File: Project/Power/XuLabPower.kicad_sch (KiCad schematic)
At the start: 24 parts, among them J1 Servo, J2 Servo, J3 Servo, J4 Servo, J5 Servo, J6 Servo, J7 Servo, J8 Servo, Q1 SQJ138ELP, Q2 SQJ138ELP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

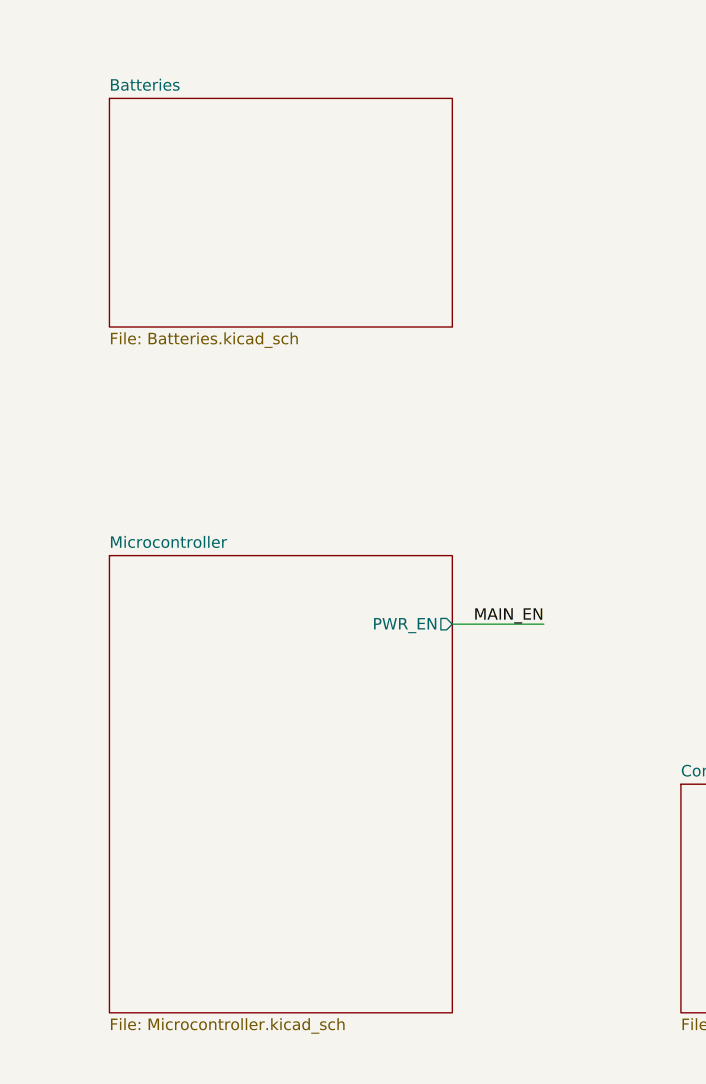
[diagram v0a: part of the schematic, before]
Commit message: Add INA226 sensors for batteries
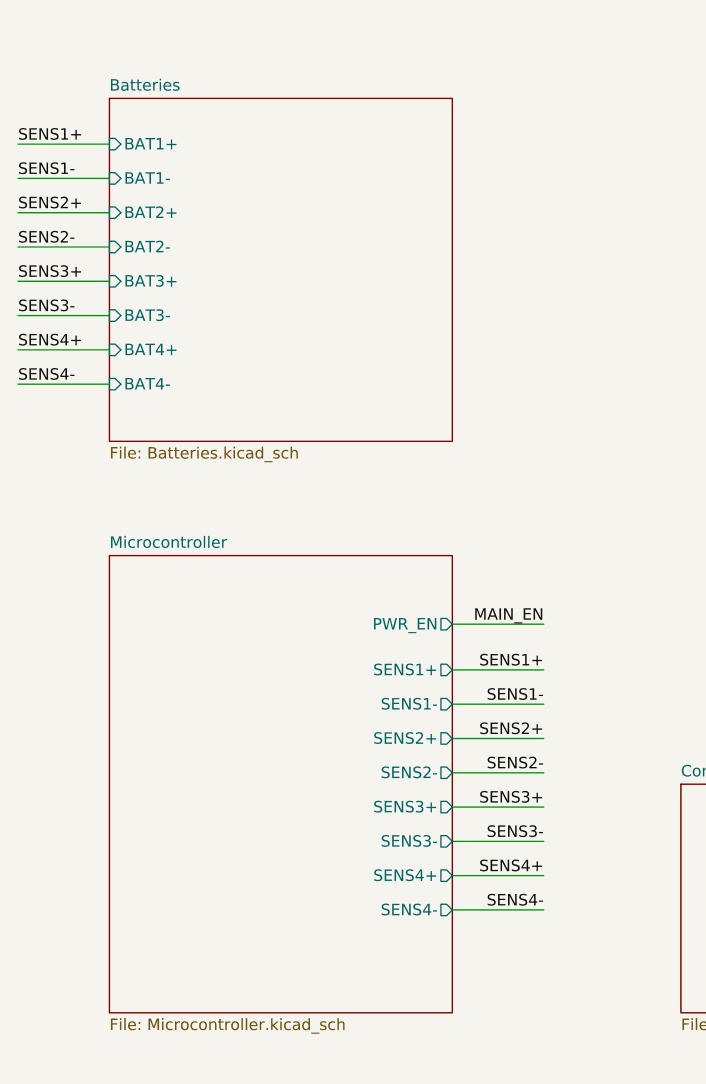
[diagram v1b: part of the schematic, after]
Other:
- sheet Batteries ports: added BAT1+, BAT1-, BAT2+, BAT2-, BAT3+, BAT3-, BAT4+, BAT4-; removed none
- sheet Microcontroller ports: added SENS1+, SENS1-, SENS2+, SENS2-, SENS3+, SENS3-, SENS4+, SENS4-; removed none

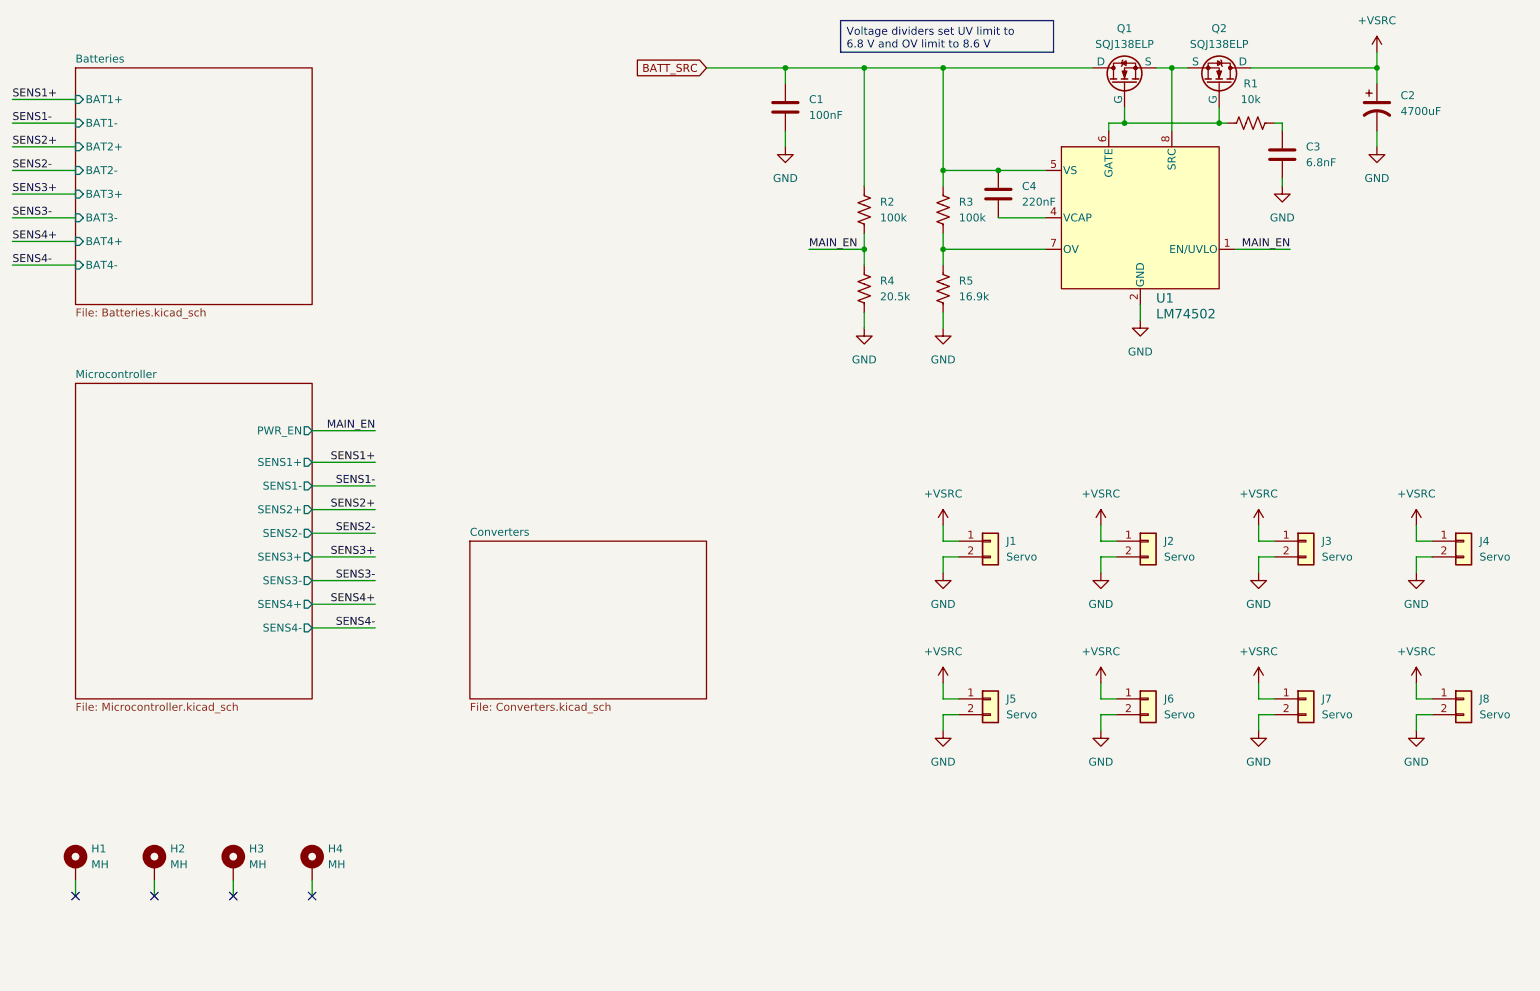
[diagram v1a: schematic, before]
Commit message: Add more sensors for fin module servos
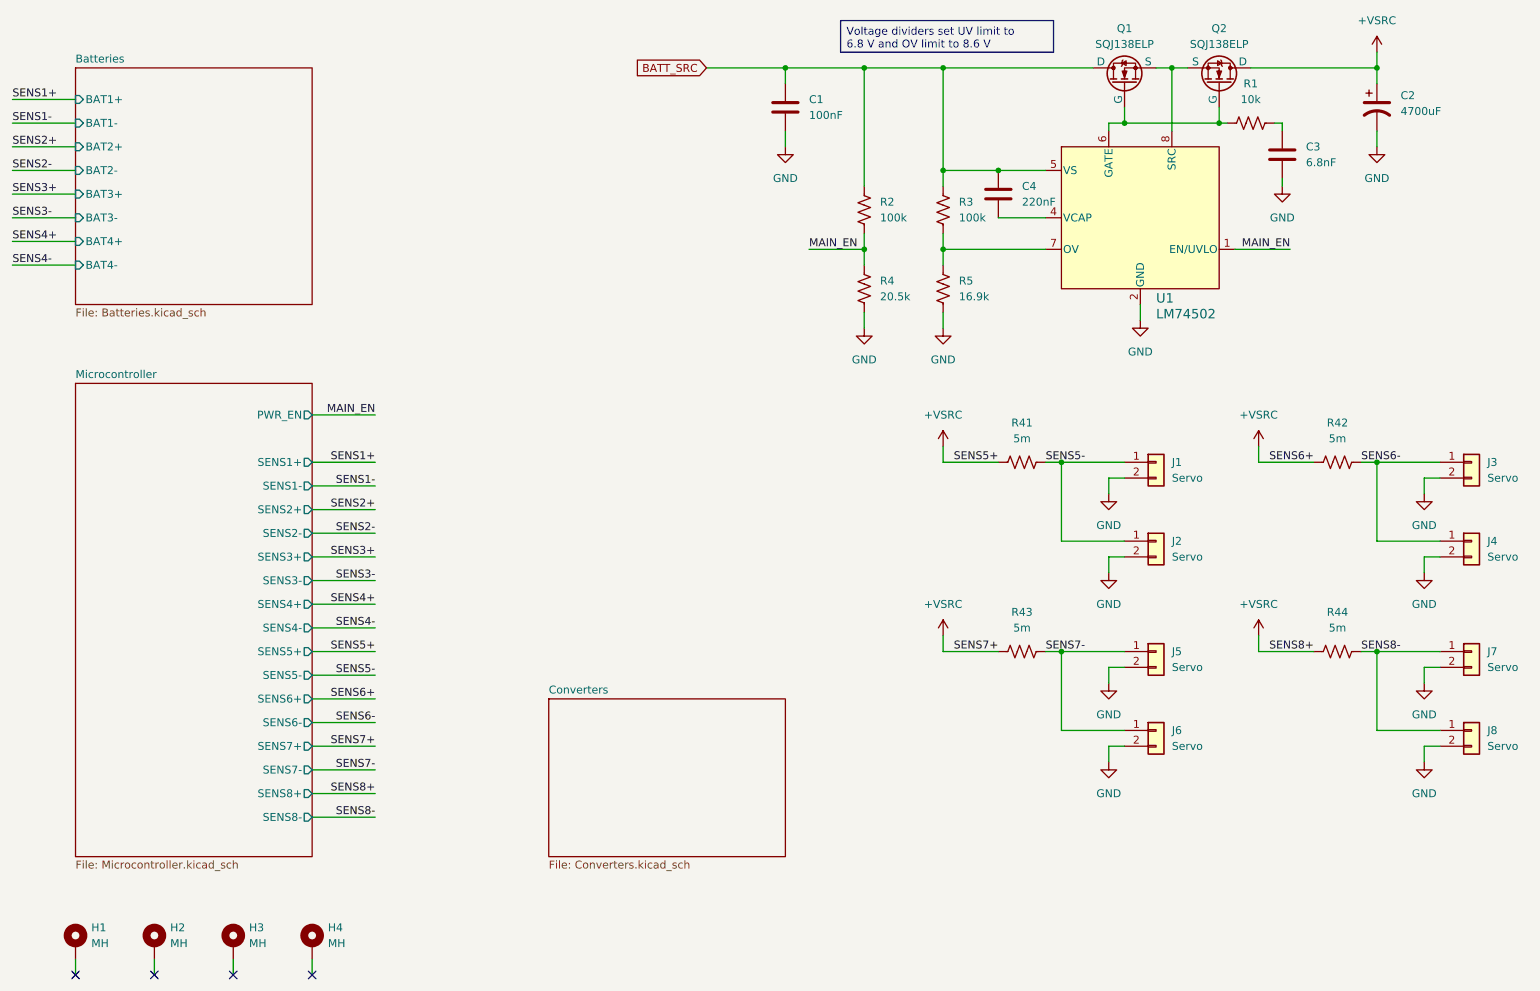
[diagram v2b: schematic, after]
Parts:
- added R41, R42, R43, R44: 5m, Resistor_SMD:R_0805_2012Metric, symbol Device:R_US
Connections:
- net +VSRC: now also R41.1, R42.1, R43.1, R44.1; no longer J1.1 (Pin_1), J2.1 (Pin_1), J3.1 (Pin_1), J4.1 (Pin_1), J5.1 (Pin_1), J6.1 (Pin_1), J7.1 (Pin_1), J8.1 (Pin_1)
- new net SENS5-: J1.1 (Pin_1), J2.1 (Pin_1), R41.2
- new net SENS6-: J3.1 (Pin_1), J4.1 (Pin_1), R42.2
- new net SENS7-: J5.1 (Pin_1), J6.1 (Pin_1), R43.2
- new net SENS8-: J7.1 (Pin_1), J8.1 (Pin_1), R44.2
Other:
- sheet Microcontroller ports: added SENS5+, SENS5-, SENS6+, SENS6-, SENS7+, SENS7-, SENS8+, SENS8-; removed none
- moved on the sheet: H1, H2, H3, H4, J1, J2

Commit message: Add TVS diodes to switch and converter outputs
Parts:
- added D7, D8: 9V, Diode_SMD:D_SMB, symbol Device:D_Zener
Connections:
- net +VSRC: now also D8.1 (K)
- net BATT_SRC: now also D7.1 (K)
- net GND: now also D7.2 (A), D8.2 (A)
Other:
- moved on the sheet: C2

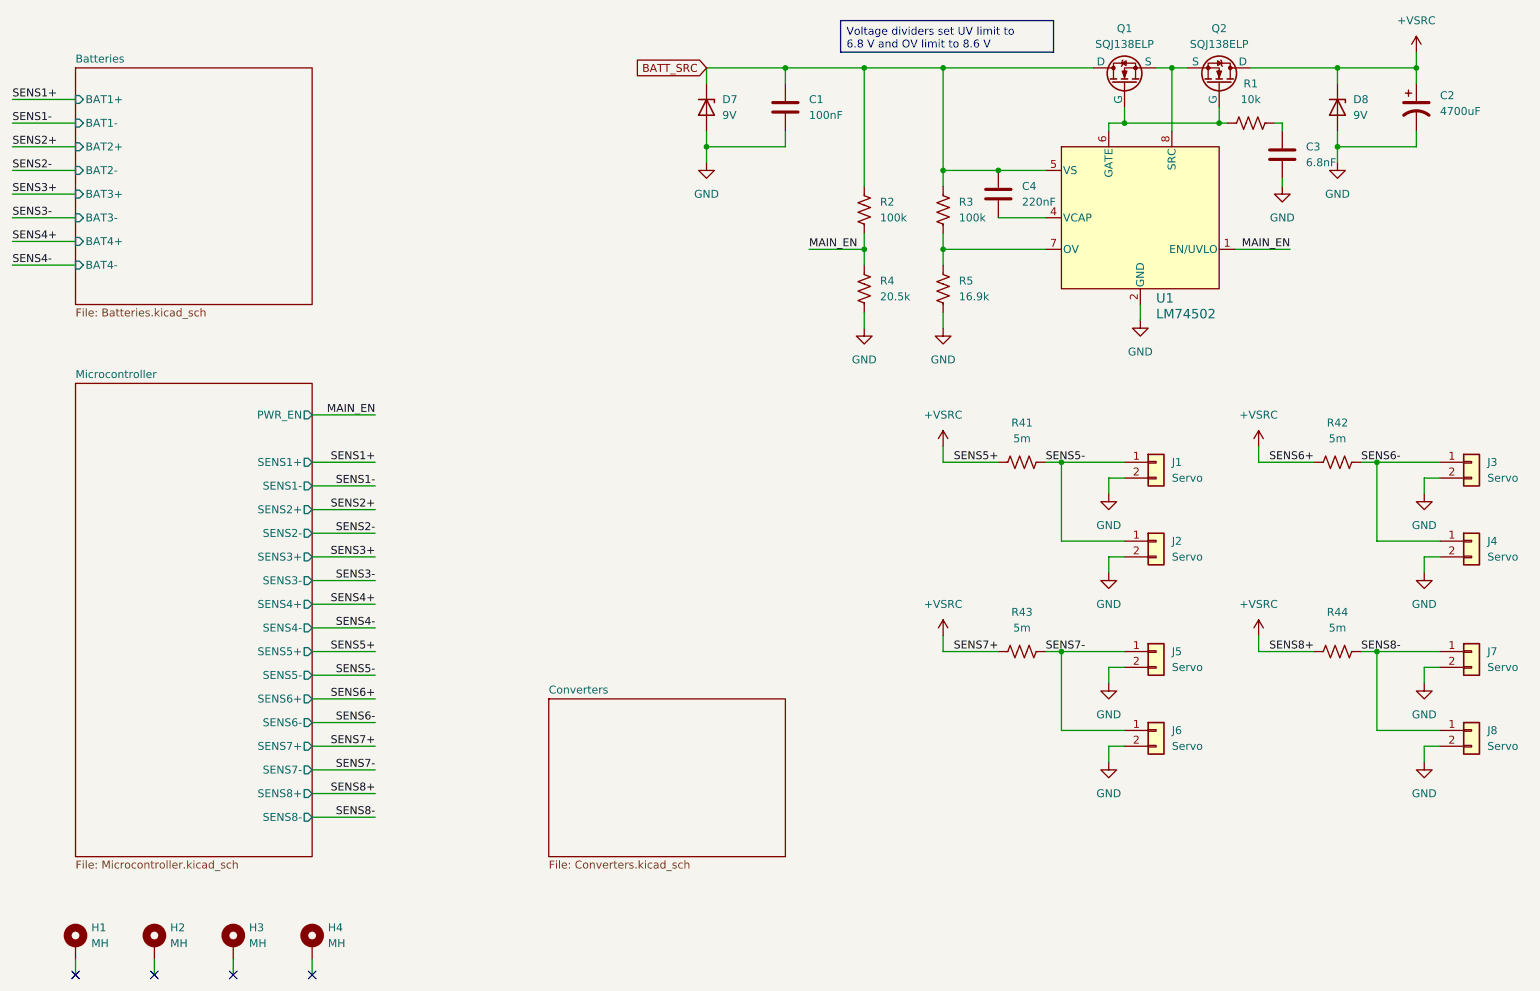
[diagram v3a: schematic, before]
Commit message: Add capacitors to servo connectors
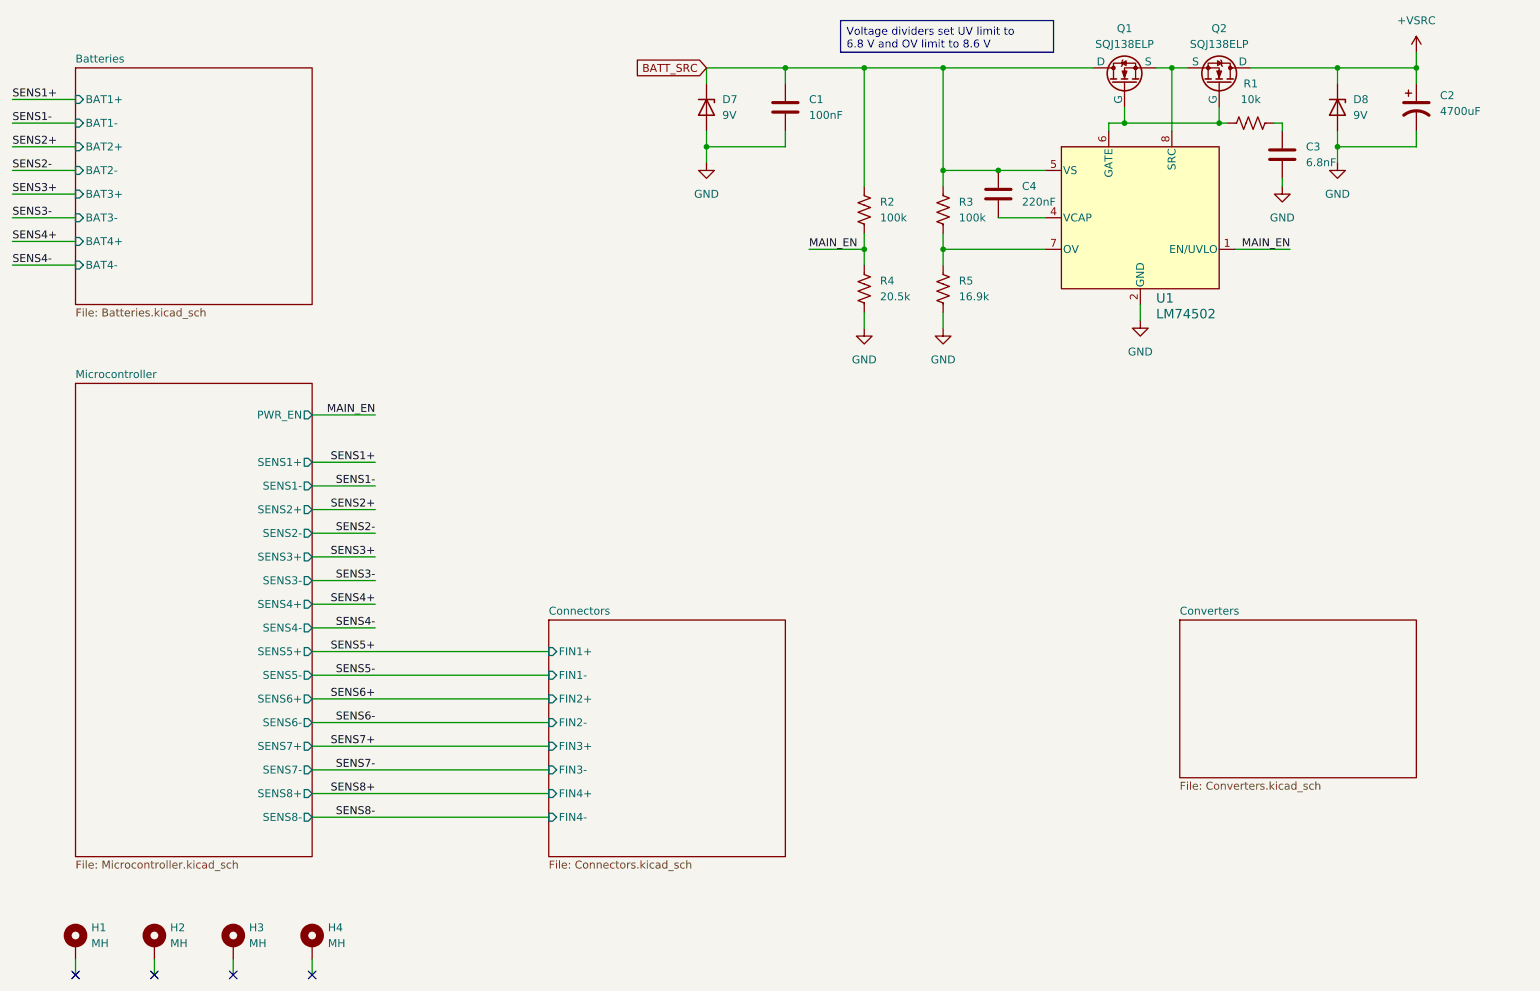
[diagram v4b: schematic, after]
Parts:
- removed J1, J2, J3, J4, J5, J6, J7, J8: Servo, Connector_JST:JST_VH_S2P-VH_1x02_P3.96mm_Horizontal, symbol Connector_Generic:Conn_01x02
- removed R41, R42, R43, R44: 5m, Resistor_SMD:R_0805_2012Metric, symbol Device:R_US
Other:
- added sheet Connectors (Connectors.kicad_sch)

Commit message: Change bulk capacitor to smaller value
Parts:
- C2: value 4700uF -> 2200uF; footprint Capacitor_THT:CP_Radial_D12.5mm_P5.00mm -> Capacitor_THT:CP_Radial_D18.0mm_P7.50mm; Listing https://www.digikey.com/en/products/detail/rubycon/16PK4700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 -> https://www.digikey.com/en/products/detail/nichicon/UHE1C22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
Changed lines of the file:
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@@
 	(title_block
 		(title "Main Sheet")
-		(date "2026-03-20")
+		(date "2026-03-24")
 		(rev "B")
 		(company "CU Boulder Senior Design Team 29 - Xu Lab")
@@
 			)
 		)
-		(property "Value" "4700uF"
+		(property "Value" "2200uF"
 			(at 257.81 45.0849 0)
 			(effects
@@
 			)
 		)
-		(property "Footprint" "Capacitor_THT:CP_Radial_D12.5mm_P5.00mm"
+		(property "Footprint" "Capacitor_THT:CP_Radial_D18.0mm_P7.50mm"
 			(at 254 44.45 0)
 			(effects
@@
 			)
 		)
-		(property "Datasheet" "https://www.rubycon.co.jp/wp-content/uploads/catalog-aluminum/PK.pdf"
+		(property "Datasheet" "https://www.nichicon.co.jp/english/series_items/catalog_pdf/e-uhe.pdf"
 			(at 254 44.45 0)
 			(effects
@@
 			)
 		)
-		(property "Listing" "https://www.digikey.com/en/products/detail/rubycon/16PK4700MEFC12-5X25/3134081"
+		(property "Listing" "https://www.digikey.com/en/products/detail/nichicon/UHE1C222MHD6/589274"
 			(at 254 44.45 0)
 			(effects
